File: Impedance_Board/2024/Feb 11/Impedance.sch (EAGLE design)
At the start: 39 parts, among them IC1 AD8608ARZ, IC2 INA826AID, U4 MC74VHC1GT66DTT1

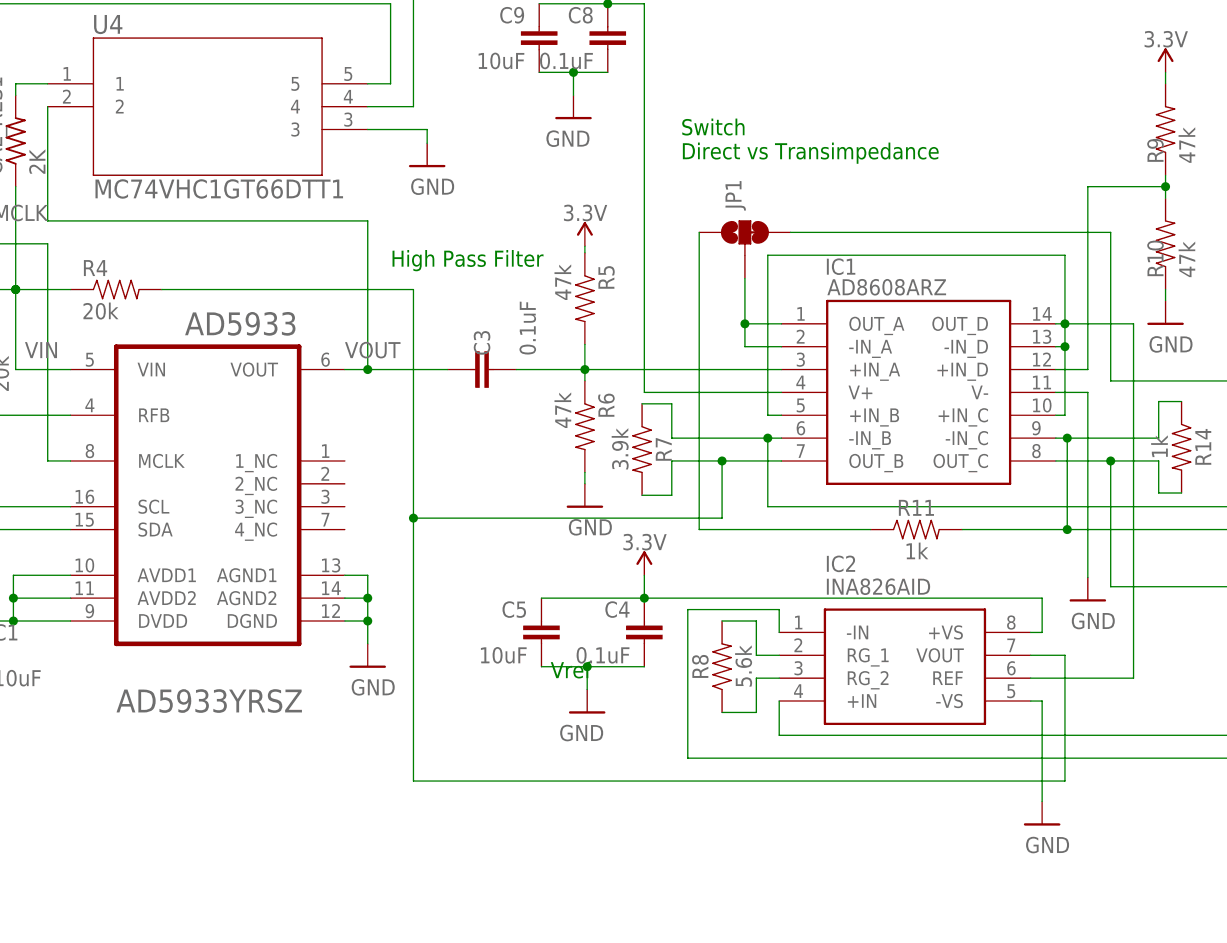
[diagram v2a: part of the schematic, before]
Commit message: Impedance update
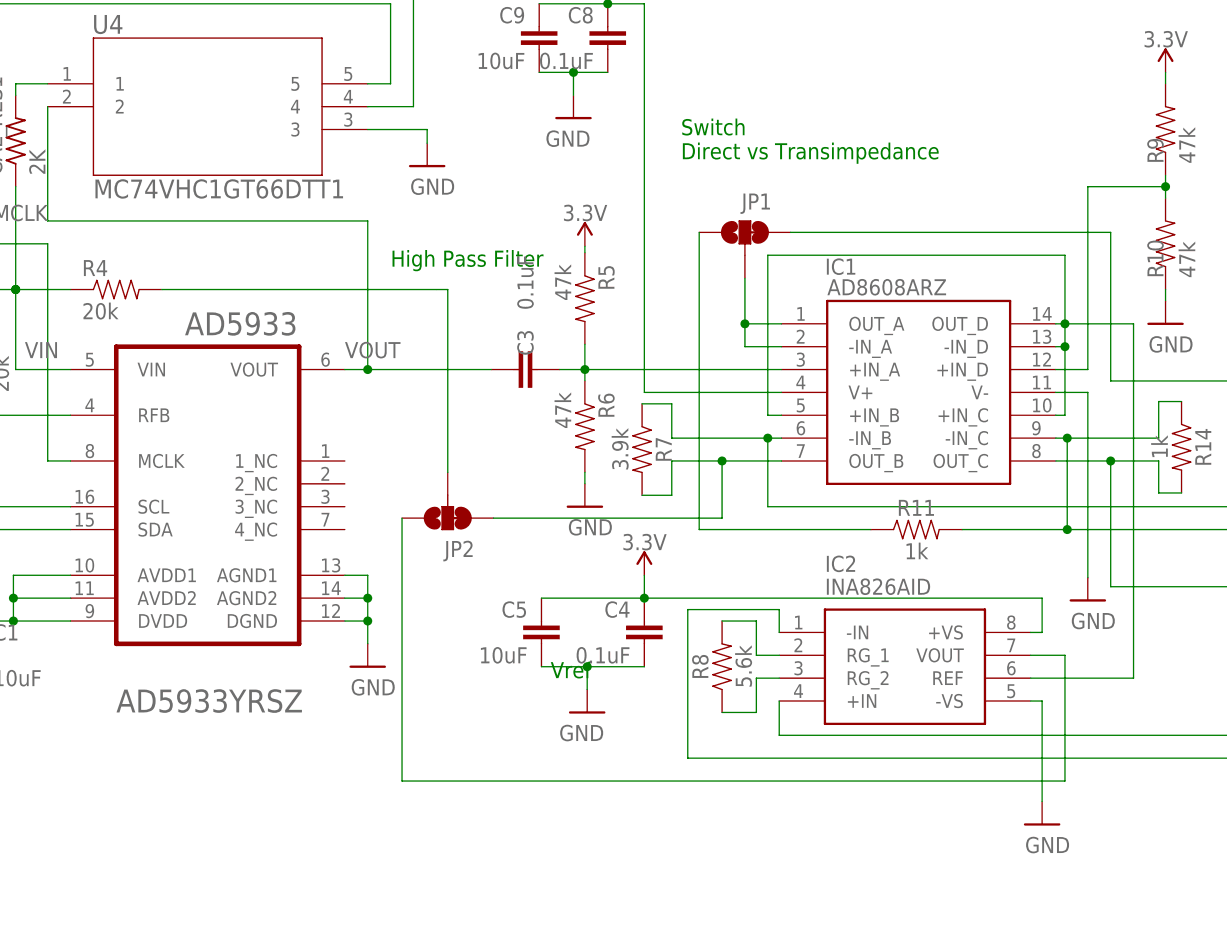
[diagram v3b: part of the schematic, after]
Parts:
- added JP2: JUMPER-SMT_3_1-NC_TRACE_NO-SILK, SparkFun-Jumpers:JUMPER-SMT_3_1-NC_TRACE_NO-SILK
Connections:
- new net N$3: IC1.OUT_B, JP2.3, R7.2
- new net N$4: JP2.2, R4.2
- net N$13: now also JP2.1; no longer IC1.OUT_B, R4.2, R7.2
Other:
- moved on the sheet: C3
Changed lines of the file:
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@@
 <setting verticaltext="up"/>
 </settings>
-<grid distance="0.1" unitdist="inch" unit="inch" style="lines" multiple="1" display="yes" altdistance="0.01" altunitdist="inch" altunit="inch"/>
+<grid distance="0.1" unitdist="inch" unit="inch" style="lines" multiple="1" display="no" altdistance="0.01" altunitdist="inch" altunit="inch"/>
 <layers>
 <layer number="1" name="Top" color="4" fill="1" visible="no" active="no"/>
@@
 <part name="SUPPLY6" library="supply1" library_urn="urn:adsk.eagle:library:371" deviceset="GND" device=""/>
 <part name="FRAME1" library="SparkFun-Aesthetics" library_urn="urn:adsk.eagle:library:507" deviceset="FRAME-LETTER" device="NO_PACKAGE" package3d_urn="urn:adsk.eagle:package:37104/1"/>
+<part name="JP2" library="SparkFun-Jumpers" library_urn="urn:adsk.eagle:library:528" deviceset="JUMPER-SMT_3_1-NC_TRACE" device="_NO-SILK" package3d_urn="urn:adsk.eagle:package:39287/1"/>
 </parts>
 <sheets>
@@
 <attribute name="VALUE" x="-41.91" y="14.478" size="1.778" layer="96"/>
 </instance>
-<instance part="C3" gate="G$1" x="3.81" y="8.89" smashed="yes" rot="R90">
-<attribute name="NAME" x="3.429" y="10.414" size="1.778" layer="95" rot="R90"/>
-<attribute name="VALUE" x="8.509" y="10.414" size="1.778" layer="96" rot="R90"/>
+<instance part="C3" gate="G$1" x="8.636" y="8.89" smashed="yes" rot="R90">
+<attribute name="NAME" x="8.255" y="10.414" size="1.778" layer="95" rot="R90"/>
+<attribute name="VALUE" x="8.255" y="15.494" size="1.778" layer="96" rot="R90"/>
 </instance>
 <instance part="R5" gate="G$1" x="13.97" y="16.764" smashed="yes" rot="R270">
@@
 </instance>
 <instance part="JP1" gate="G$1" x="31.75" y="24.13" smashed="yes" rot="R90">
-<attribute name="NAME" x="31.369" y="26.67" size="1.778" layer="95" font="vector" rot="R90"/>
+<attribute name="NAME" x="31.369" y="26.67" size="1.778" layer="95" font="vector"/>
 <attribute name="VALUE" x="32.131" y="26.67" size="1.778" layer="96" font="vector" rot="R90" align="top-left" display="off"/>
 </instance>
@@
 <attribute name="SHEET" x="109.22" y="-97.79" size="2.54" layer="94" font="vector"/>
 <attribute name="DRAWING_NAME" x="38.354" y="-81.28" size="2.7432" layer="94" font="vector"/>
+</instance>
+<instance part="JP2" gate="G$1" x="-1.27" y="-7.62" smashed="yes" rot="MR270">
+<attribute name="NAME" x="-1.651" y="-10.16" size="1.778" layer="95" font="vector" rot="MR180"/>
+<attribute name="VALUE" x="-0.889" y="-10.16" size="1.778" layer="96" font="vector" rot="MR270" align="top-left" display="off"/>
 </instance>
 </instances>
@@
 <pinref part="AD5933" gate="G$0" pin="VOUT"/>
 <pinref part="C3" gate="G$1" pin="1"/>
-<wire x1="-1.27" y1="8.89" x2="-10.16" y2="8.89" width="0.1524" layer="91"/>
+<wire x1="3.556" y1="8.89" x2="-10.16" y2="8.89" width="0.1524" layer="91"/>
 <pinref part="U4" gate="A" pin="2"/>
 <wire x1="-10.16" y1="8.89" x2="-12.7" y2="8.89" width="0.1524" layer="91"/>
@@
 <segment>
 <pinref part="C3" gate="G$1" pin="2"/>
-<wire x1="6.35" y1="8.89" x2="13.97" y2="8.89" width="0.1524" layer="91"/>
+<wire x1="11.176" y1="8.89" x2="13.97" y2="8.89" width="0.1524" layer="91"/>
 <pinref part="R6" gate="G$1" pin="1"/>
 <wire x1="13.97" y1="8.89" x2="13.97" y2="7.62" width="0.1524" layer="91"/>
@@
 <net name="N$13" class="0">
 <segment>
+<wire x1="-6.35" y1="-36.83" x2="67.31" y2="-36.83" width="0.1524" layer="91"/>
+<wire x1="67.31" y1="-36.83" x2="67.31" y2="-22.86" width="0.1524" layer="91"/>
+<pinref part="IC2" gate="G$1" pin="VOUT"/>
+<wire x1="67.31" y1="-22.86" x2="63.5" y2="-22.86" width="0.1524" layer="91"/>
+<pinref part="JP2" gate="G$1" pin="1"/>
+<wire x1="-6.35" y1="-36.83" x2="-6.35" y2="-7.62" width="0.1524" layer="91"/>
+</segment>
+</net>
+<net name="N$3" class="0">
+<segment>
+<pinref part="IC1" gate="G$1" pin="OUT_B"/>
+<wire x1="29.21" y1="-7.62" x2="29.21" y2="-1.27" width="0.1524" layer="91"/>
+<wire x1="29.21" y1="-1.27" x2="35.814" y2="-1.27" width="0.1524" layer="91"/>
+<junction x="29.21" y="-1.27"/>
+<wire x1="23.622" y1="-1.27" x2="29.21" y2="-1.27" width="0.1524" layer="91"/>
 <wire x1="23.622" y1="-5.08" x2="23.622" y2="-1.27" width="0.1524" layer="91"/>
 <pinref part="R7" gate="G$1" pin="2"/>
 <wire x1="20.32" y1="-5.08" x2="23.622" y2="-5.08" width="0.1524" layer="91"/>
-<pinref part="IC1" gate="G$1" pin="OUT_B"/>
-<wire x1="29.21" y1="-7.62" x2="29.21" y2="-1.27" width="0.1524" layer="91"/>
-<wire x1="29.21" y1="-1.27" x2="35.814" y2="-1.27" width="0.1524" layer="91"/>
+<pinref part="JP2" gate="G$1" pin="3"/>
+<wire x1="29.21" y1="-7.62" x2="3.81" y2="-7.62" width="0.1524" layer="91"/>
+</segment>
+</net>
+<net name="N$4" class="0">
+<segment>
 <pinref part="R4" gate="G$1" pin="2"/>
-<wire x1="-33.02" y1="17.78" x2="-5.08" y2="17.78" width="0.1524" layer="91"/>
-<wire x1="-5.08" y1="17.78" x2="-5.08" y2="-7.62" width="0.1524" layer="91"/>
-<wire x1="-5.08" y1="-7.62" x2="-5.08" y2="-36.83" width="0.1524" layer="91"/>
-<wire x1="-5.08" y1="-36.83" x2="67.31" y2="-36.83" width="0.1524" layer="91"/>
-<wire x1="67.31" y1="-36.83" x2="67.31" y2="-22.86" width="0.1524" layer="91"/>
-<pinref part="IC2" gate="G$1" pin="VOUT"/>
-<wire x1="67.31" y1="-22.86" x2="63.5" y2="-22.86" width="0.1524" layer="91"/>
-<wire x1="29.21" y1="-7.62" x2="-5.08" y2="-7.62" width="0.1524" layer="91"/>
-<junction x="-5.08" y="-7.62"/>
-<wire x1="23.622" y1="-1.27" x2="29.21" y2="-1.27" width="0.1524" layer="91"/>
-<junction x="29.21" y="-1.27"/>
-</segment>
-</net>
+<wire x1="-33.02" y1="17.78" x2="-2.54" y2="17.78" width="0.1524" layer="91"/>
+<pinref part="JP2" gate="G$1" pin="2"/>
+<wire x1="-1.27" y1="-2.54" x2="-1.27" y2="17.78" width="0.1524" layer="91"/>
+<wire x1="-1.27" y1="17.78" x2="-2.54" y2="17.78" width="0.1524" layer="91"/>
+</segment>
+</net>
